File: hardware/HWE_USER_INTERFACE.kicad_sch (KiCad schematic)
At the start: 14 parts, among them J10 OLED_DISPLAY_i2c, J11 ENC_VOLUME_LED-RING, J13 OLED_DISPLAY_SPI, J4 BTN_PLAY, J5 BTN_REC, J6 BTN_STOP, J7 BTN_QUANTISE, J8 BTN_OVERDUB, J9 BTN_METRONOME

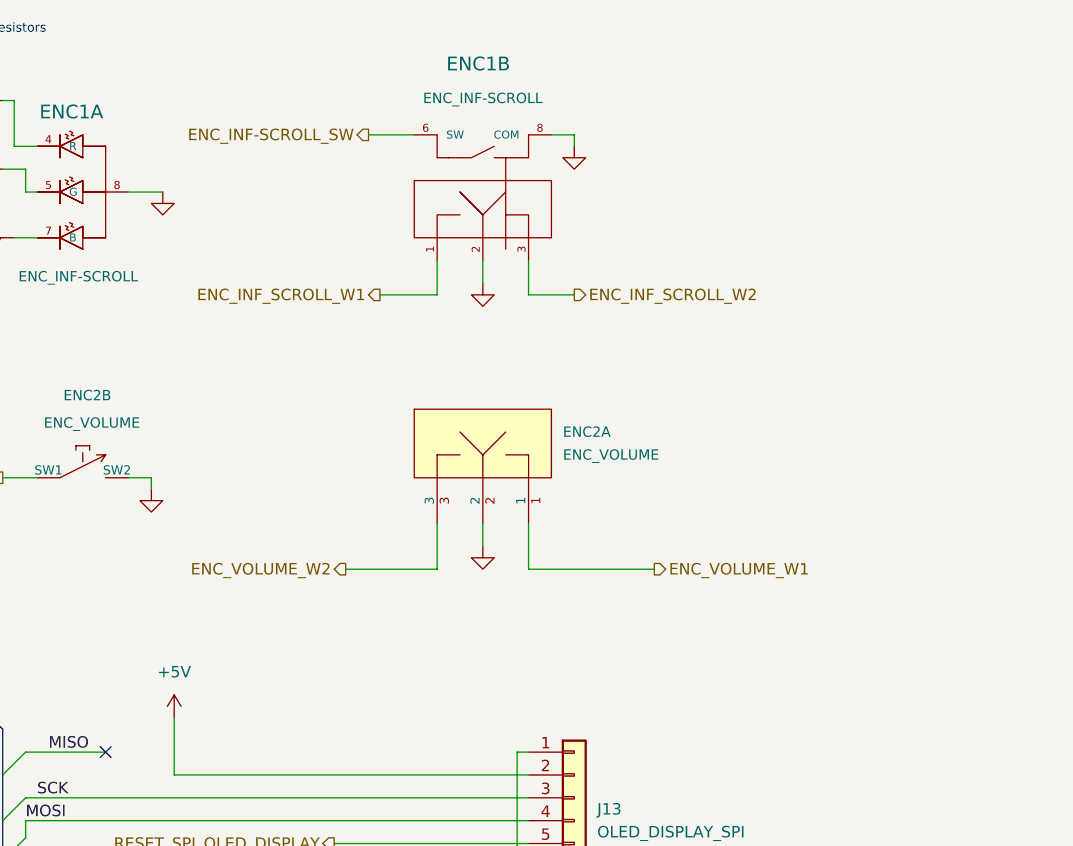
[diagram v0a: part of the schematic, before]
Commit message: fix [HWE]: Reassigned Rot Enc outs to new MCU GPIO
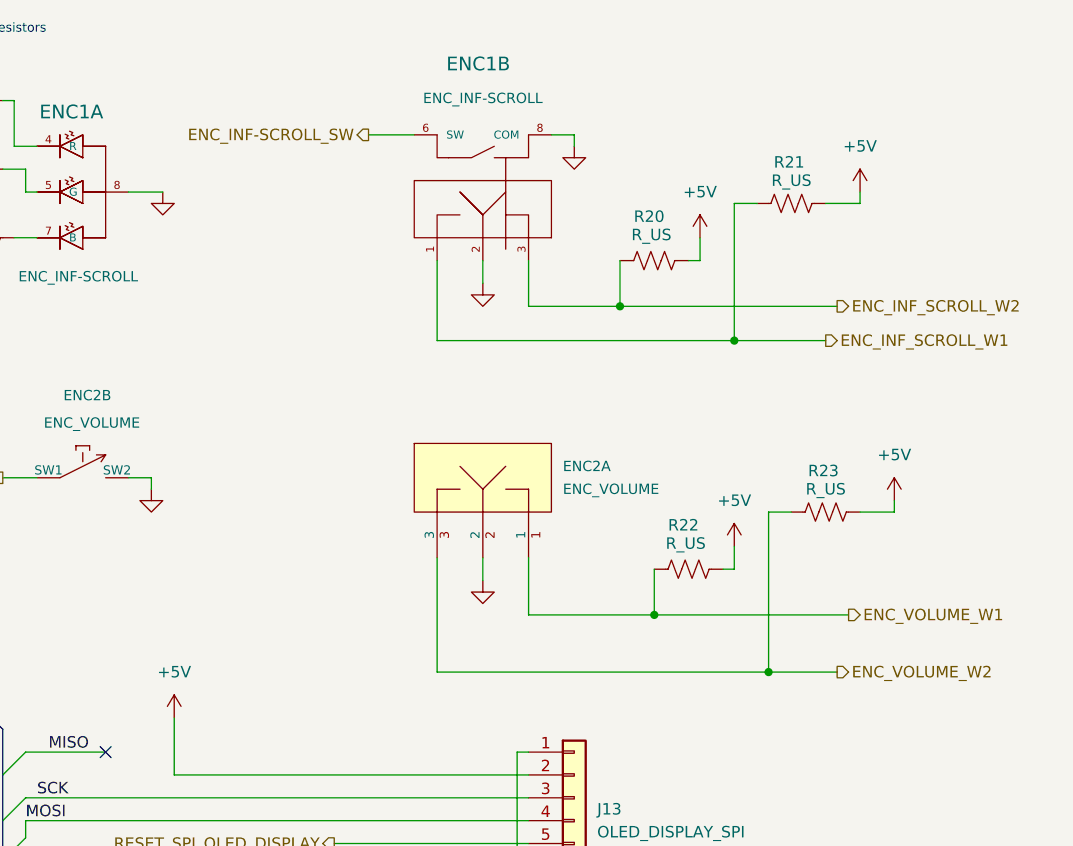
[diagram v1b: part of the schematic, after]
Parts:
- added R20, R21, R22, R23: R_US, symbol Device:R_US
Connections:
- net +5V: now also R20.2, R21.2, R22.2, R23.2
- net ENC_INF_SCROLL_W1: now also R21.1
- net ENC_INF_SCROLL_W2: now also R20.1
- net ENC_VOLUME_W1: now also R22.1
- net ENC_VOLUME_W2: now also R23.1
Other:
- moved on the sheet: ENC2A

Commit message: feat![HWE]: Changed MCU to Adafruit ESP32-S3
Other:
- company: (none) -> Madueke Systems and Technologies
- title: (none) -> Simple Midi Transport Controller
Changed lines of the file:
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@@
 	(generator_version "9.0")
 	(paper "A4")
+	(title_block
+		(title "Simple Midi Transport Controller")
+		(date "2026-04-06")
+		(rev "1")
+		(company "Madueke Systems and Technologies")
+		(comment 1 "Used the combination of the Adafruit Feather ESP32-V2 Dev Board and the SX1509 IO expander")
+	)
 	(text "Current-limiting Resistors"
 		(exclude_from_sim no)
@@
 			"AAAAAAAAAAAAAAAAAAAAAAAAAAAAAAAAAAAAAAAAAAAAAAAAAAAAAAAAAAAAAAAAAAAAAAAAAAAA"
 			"AAAAAAAAAAAAAAAAAAAAAAAAAAAAAAAAAAAAAAAAAAAAAAAAAAAAAAAAAAAAAAAAAAAAAAAAAAAA"
-			"AAAAAAAAAAAAAAAAAAAAAAAAAAAAAAAAAAAAAAAAAAAAAAAAAAAAAAAAAAAAAAAAAAAAAAAAAA=="
-		)
-	)
+			"AAAAAAAAAAAAAAAAAAAAAAAAAAAAAAAAAAAAAAAAAAAAAAAAAAAAAAAAAAAAAAAAAAAAAAAAALg+"
+			"AFcEgAAAAAAAAAAACAAAAAAAAACAHP6VcgEAAAEAAAAAAAAAAAAAAAAAAACxFbs+AFgEgAAAAAAA"
+			"AAAAAwAAAAAAAACgREmWcgEAAAEAAAAAAAAAAAAAAAAAAAC0FbY+AFkEgGCYTJZyAQAAAwAAAAAA"
+			"AADgSUmWcgEAAAEAAAAAAAAAAAAAAAAAAAC3FbE+AFoEgAAAAAAAAAAAAwAAAAAAAADwlUyWcgEA"
+			"AAEAAAAAAAAAAAAAAAAAAACKFYw+AFsEgAAAAAAAAAAACAAAAAAAAAAAHv6VcgEAAAEAAAAAAAAA"
+			"AAAAAAAAAACNFY8+AFwEgCCNTJZyAQAAAwAAAAAAAACATkmWcgEAAAEAAAAAAAAAAAAAAAAAAACA"
+			"FYo+AF0EgECOTJZyAQAAAwAAAAAAAADg+UyWcgEAAAEAAAAAAAAAAAAAAAAAAACDFYU+AF4EgHCU"
+			"TJZyAQAAAwAAAAAAAACQ/EyWcgEAAAEAAAAAAAAAAAAAAAAAAACGFYA+AF8EgAAAAAAAAAAAAwAA"
+			"AAAAAAAA/EyWcgEAAAEAAAAAAAAAAAAAAAAAAACZFYM+AGAEgMCVTJZyAQAAAwAAAAAAAADw90yW"
+			"cgEAAAEAAAAAAAAAAAAAAAAAAACcFZ4+AGEEgAAAAAAAAAAABAAAAAAAAAABAAAAAAAAAAEAAAAA"
+			"AAAAAAAAAAAAAACfFZk+AGIEgBCUTJZyAQAAAwAAAAAAAACgSkmWcgEAAAEAAAAAAAAAAAAAAAAA"
+			"AACSFZQ+AGMEgAAAAAAAAAAAAwAAAAAAAACAjUyWcgEAAAEAAAAAAAAAAAAAAAAAAACVFZc+AGQE"
+			"gEM6L1dJTkRPV1MvZm9udHNcbXNnb3RoaWMudHRjAAAAAAAAAAAAAADoFZI+AGUEgECUTJZyAQAA"
+			"AwAAAAAAAACgTEmWcgEAAAEAAAAAAAAAAAAAAAAAAADrFe0+AGYEgKCUTJZyAQAAAwAAAAAAAACg"
+			"TkmWcgEAAAEAAAAAAAAAAAAAAAAAAADuFeg+AGcEgGCPTJZyAQAAAwAAAAAAAADw+0yWcgEAAAEA"
+			"AAAAAAAAAAAAAAAAAADhFes+AGgEgACeTJZyAQAAAwAAAAAAAABgTEmWcgEAAAEAAAAAAAAAAAAA"
+			"AAAAAADkFeY+AGkEgAAAAAAAAAAACAAAAAAAAADAGf6VcgEAAAEAAAAAAAAAAAAAAAAAAADnFeE+"
+			"AGoEgICTTJZyAQAAAwAAAAAAAACA/EyWcgEAAAEAAAAAAAAAAAAAAAAAAAD6Ffw+AGsEgNCXTJZy"
+			"AQAAAwAAAAAAAAAASUmWcgEAAAEAAAAAAAAAAAAAAAAAAAD9Ff8+AGwEgAAAAAAAAAAACAAAAA=="
+		)
+	)

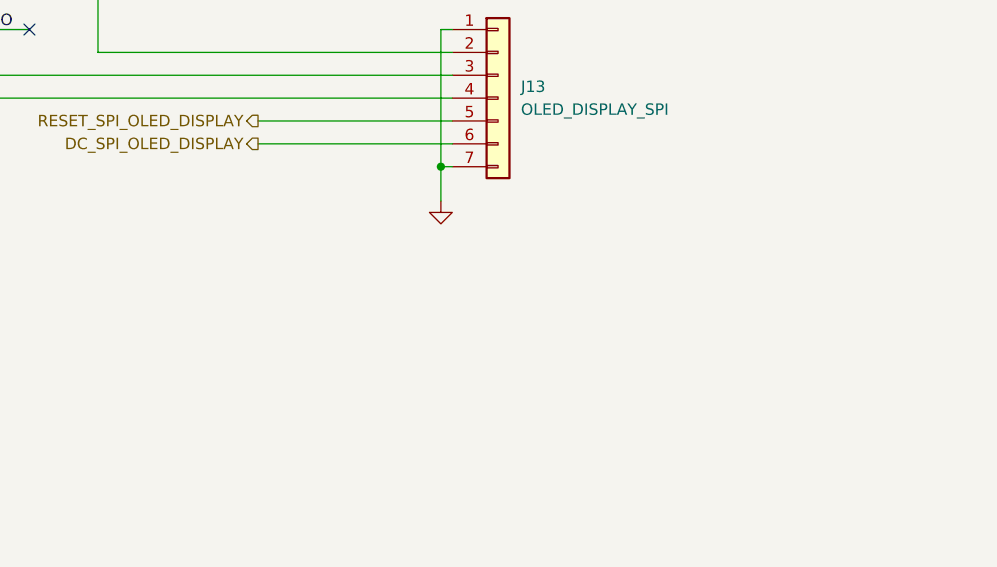
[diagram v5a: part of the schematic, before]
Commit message: misc [HWE]: Clarified Pin Status of SPI OLED display
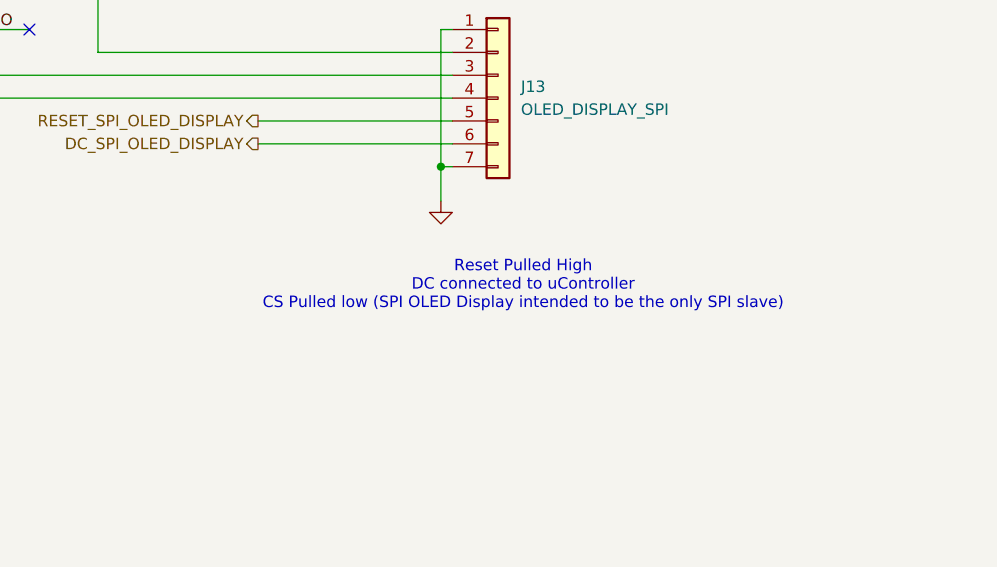
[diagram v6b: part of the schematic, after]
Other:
- note added: "Reset Pulled High DC connected to uController CS Pulled low (SPI OLED Display intended to be the only SPI slave)"
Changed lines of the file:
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@@
+		)
+	)
+	(text "Reset Pulled High\nDC connected to uController\nCS Pulled low (SPI OLED Display intended to be the only SPI slave)"
+		(exclude_from_sim no)
+		(at 236.474 124.968 0)
+		(effects
+			(font
+				(size 1.27 1.27)
+			)
 		)
 	)

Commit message: fix [HWE]: Update SPI OLED RES and DC connections
The RES pin of the OLED display is now connected to the RESET pin of the MCU, the DC pin will be routed to the GPIO pin D13 (at the cost of continually driving the BUILITIN LED)
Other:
- note added: "Reset connected to uController RESET DC connected to uController CS Pulled low (SPI OLED Display intended to be the only SPI slave)"
- note removed: "Reset Pulled High DC connected to uController CS Pulled low (SPI OLED Display intended to be the only SPI slave)"
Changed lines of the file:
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@@
 		)
 	)
-	(text "Reset Pulled High\nDC connected to uController\nCS Pulled low (SPI OLED Display intended to be the only SPI slave)"
+	(text "Reset connected to uController RESET\nDC connected to uController\nCS Pulled low (SPI OLED Display intended to be the only SPI slave)"
 		(exclude_from_sim no)
 		(at 236.474 124.968 0)

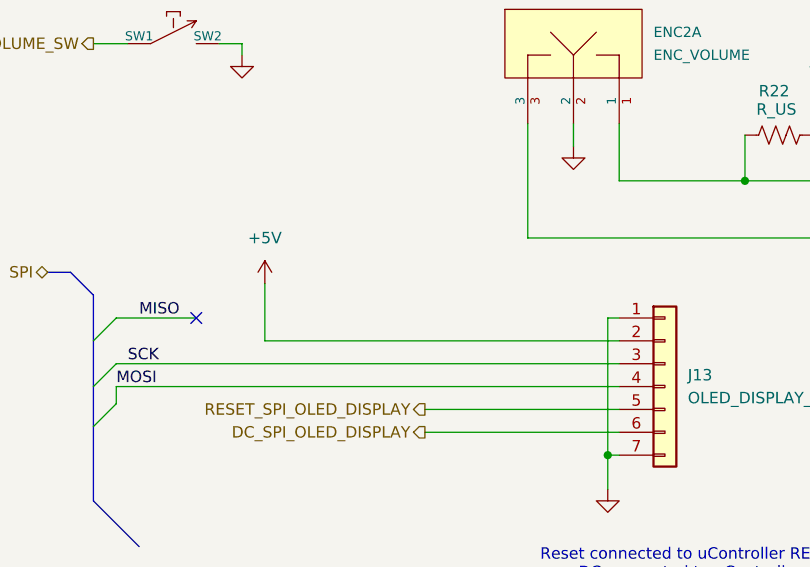
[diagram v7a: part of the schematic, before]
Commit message: feat [HWE]: Added probe points to SPI connections
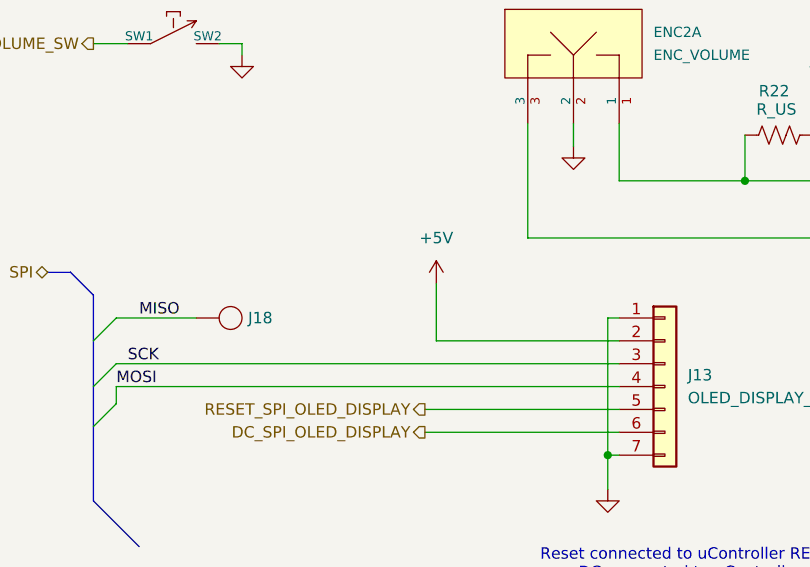
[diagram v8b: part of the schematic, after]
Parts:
- added J18: ~, 4ms_Connector:CAPSENSE_PAD, symbol 4ms_Connector:CAPSENSE_PAD
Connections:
- net MISO: now also J18.1 (CS)
- no-connect marks 1 -> 0
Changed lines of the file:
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@@
 		(color 0 0 0 0)
 	)
-	(no_connect
-		(at 181.61 96.52)
-	)
 	(bus_entry
 		(at 170.18 99.06)
@@
 	(wire
 		(pts
-			(xy 189.23 99.06) (xy 228.6 99.06)
+			(xy 208.28 99.06) (xy 228.6 99.06)
 		)
 		(stroke
@@
 	(wire
 		(pts
-			(xy 189.23 92.71) (xy 189.23 99.06)
+			(xy 208.28 92.71) (xy 208.28 99.06)
 		)
 		(stroke
@@
 	(symbol
 		(lib_id "4ms_Power-symbol:+5V")
-		(at 189.23 92.71 0)
+		(at 208.28 92.71 0)
 		(unit 1)
 		(exclude_from_sim no)
@@
 		(fields_autoplaced yes)
 		(property "Reference" "#PWR048"
-			(at 189.23 96.52 0)
+			(at 208.28 96.52 0)
 			(effects
 				(font
@@
 		)
 		(property "Value" "+5V"
-			(at 189.23 87.63 0)
+			(at 208.28 87.63 0)
 			(effects
 				(font
@@
 		)
 		(property "Footprint" ""
-			(at 189.23 92.71 0)
+			(at 208.28 92.71 0)
 			(effects
 				(font
@@
 		)
 		(property "Datasheet" ""
-			(at 189.23 92.71 0)
+			(at 208.28 92.71 0)
 			(effects
 				(font
@@
 		)
 		(property "Description" ""
-			(at 189.23 92.71 0)
+			(at 208.28 92.71 0)
 			(effects
 				(font
@@
 					(unit 1)
 				)
+			)
+		)
+	)
+	(symbol
+		(lib_id "4ms_Connector:CAPSENSE_PAD")
+		(at 185.42 96.52 0)
+		(unit 1)
+		(exclude_from_sim no)
+		(in_bom yes)
+		(on_board yes)
+		(dnp no)
+		(property "Reference" "J18"
+			(at 188.722 96.52 0)
+			(effects
+				(font
+					(size 1.27 1.27)
+				)
+			)
+		)
+		(property "Value" "~"
+			(at 185.42 99.06 0)
+			(effects
+				(font
+					(size 1.27 1.27)
+				)
+				(hide yes)
+			)
+		)
+		(property "Footprint" "4ms_Connector:CAPSENSE_PAD"
+			(at 195.326 101.6 0)
+			(effects
+				(font
+					(size 1.27 1.27)
+				)
+				(hide yes)
+			)
+		)
+		(property "Datasheet" ""
+			(at 185.42 96.52 0)
+			(effects
+				(font
+					(size 1.27 1.27)
+				)
+				(hide yes)
+			)
+		)
+		(property "Description" ""
+			(at 185.42 96.52 0)
+			(effects
+				(font
+					(size 1.27 1.27)
+				)
+				(hide yes)
+			)
+		)
+		(pin "1"
+		)
+		(instances
+			(project "10032025_01_[HWE] Simple Transport Midi Controller"
+				(path "/4f4cdf46-015d-4b38-9cc1-de7a767260f6/96b58b50-e06e-4f86-ba39-1d02b5cd5477"
+					(reference "J18")
+					(unit 1)
+				)
